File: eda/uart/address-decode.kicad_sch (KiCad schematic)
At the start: 2 parts, among them U6 74HCT139

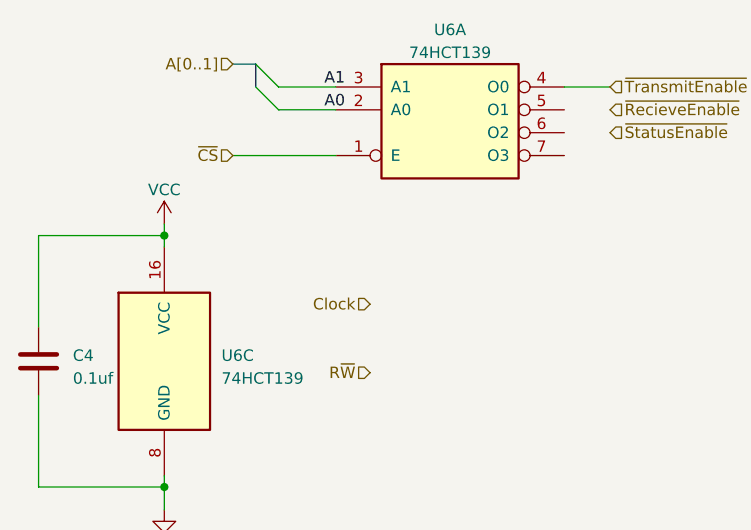
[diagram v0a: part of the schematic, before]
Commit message: Port main board schematic to kicad
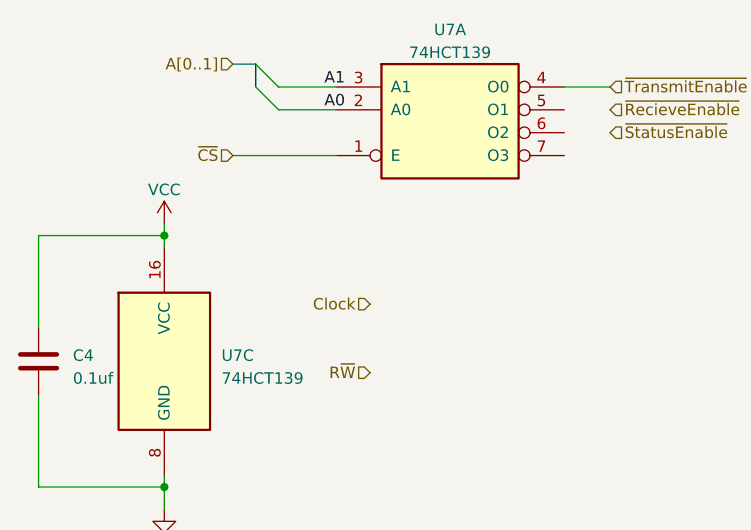
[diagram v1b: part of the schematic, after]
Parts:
- C4: footprint Capacitor_THT:C_Rect_L7.2mm_W2.5mm_P5.00mm_FKS2_FKP2_MKS2_MKP2 -> Capacitor_THT:C_Rect_L7.2mm_W3.5mm_P5.00mm_FKS2_FKP2_MKS2_MKP2
- renumbered U6 to U7
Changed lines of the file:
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@@
         )
         (path "/11545594-d6d6-4b37-a578-fa23933d5773/6450b7fb-1287-48ad-899d-2faf7b3277a5"
-          (reference "#PWR021") (unit 1)
+          (reference "#PWR023") (unit 1)
         )
       )
@@
         )
         (path "/11545594-d6d6-4b37-a578-fa23933d5773/6450b7fb-1287-48ad-899d-2faf7b3277a5"
-          (reference "#PWR022") (unit 1)
+          (reference "#PWR024") (unit 1)
         )
       )
@@
       (effects (font (size 1.27 1.27)) (justify left))
     )
-    (property "Footprint" "Capacitor_THT:C_Rect_L7.2mm_W2.5mm_P5.00mm_FKS2_FKP2_MKS2_MKP2" (at 20.0152 74.93 0)
+    (property "Footprint" "Capacitor_THT:C_Rect_L7.2mm_W3.5mm_P5.00mm_FKS2_FKP2_MKS2_MKP2" (at 20.0152 74.93 0)
       (effects (font (size 1.27 1.27)) hide)
     )
@@
         )
         (path "/11545594-d6d6-4b37-a578-fa23933d5773/6450b7fb-1287-48ad-899d-2faf7b3277a5"
-          (reference "C9") (unit 1)
+          (reference "C10") (unit 1)
         )
       )
@@
   (symbol (lib_id "74xx:74LS139") (at 33.02 71.12 0) (unit 3)
     (in_bom yes) (on_board yes) (dnp no) (fields_autoplaced)
-    (property "Reference" "U6" (at 39.37 70.485 0)
+    (property "Reference" "U7" (at 39.37 70.485 0)
       (effects (font (size 1.27 1.27)) (justify left))
     )
@@
       (project "uart"
         (path "/11545594-d6d6-4b37-a578-fa23933d5773/6450b7fb-1287-48ad-899d-2faf7b3277a5"
-          (reference "U6") (unit 3)
+          (reference "U7") (unit 3)
         )
       )
@@
   (symbol (lib_id "74xx:74LS139") (at 64.77 43.18 0) (unit 1)
     (in_bom yes) (on_board yes) (dnp no) (fields_autoplaced)
-    (property "Reference" "U6" (at 64.77 34.29 0)
+    (property "Reference" "U7" (at 64.77 34.29 0)
       (effects (font (size 1.27 1.27)))
     )
@@
       (project "uart"
         (path "/11545594-d6d6-4b37-a578-fa23933d5773/6450b7fb-1287-48ad-899d-2faf7b3277a5"
-          (reference "U6") (unit 1)
+          (reference "U7") (unit 1)
         )
       )

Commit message: Update eda
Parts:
- added U15: 74HCT00, symbol 74xx:74HCT00
- added U18: 74HCT32, Package_DIP:DIP-14_W7.62mm, symbol 74xx:74LS32
- added U2 (x3): 74HCT14, Package_DIP:DIP-14_W7.62mm, symbol 74xx:74LS14
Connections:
- net Clock: now also U15.2
- net R~{W}: now also U2.1
- net ~{CS}: now also U2.1; no longer U7.1 (E)
- net ~{RecieveEnable}: now also U18.3
- net ~{StatusEnable}: now also U18.6
- net at U7.5 (O1): now also U18.1
- net at U7.6 (O2): now also U18.4
- net ~{TransmitEnable}: no longer names the net of U7.4 (O0)
- net ~{TransmitEnable}: now also U2.1
- new net: U18.2, U18.5, U2.2
- new net: U15.1, U2.2
- new net: U15.3, U7.1 (E)
- new net TransmitEnable: U2.2
- no-connect marks 0 -> 1
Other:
- moved on the sheet: U7A

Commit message: Convert expansion breakout to kicad
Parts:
- U15: footprint (none) -> Package_DIP:DIP-14_W7.62mm
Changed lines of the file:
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@@
       (effects (font (size 1.27 1.27)))
     )
-    (property "Footprint" "" (at 83.82 42.545 0)
+    (property "Footprint" "Package_DIP:DIP-14_W7.62mm" (at 83.82 42.545 0)
       (effects (font (size 1.27 1.27)) hide)
     )

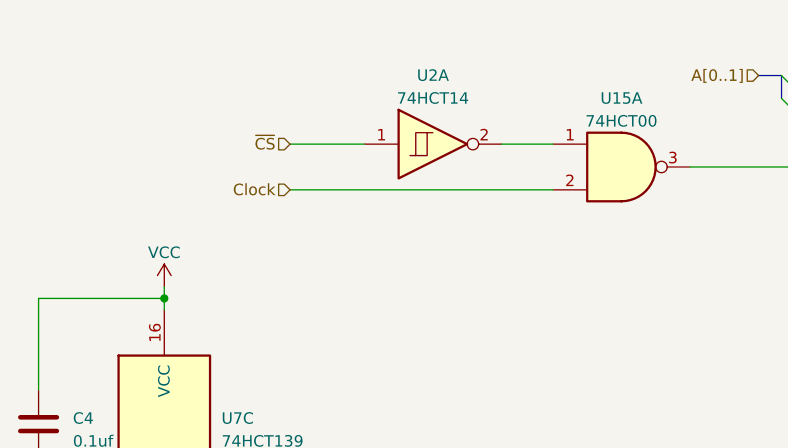
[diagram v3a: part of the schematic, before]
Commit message: Prelimary UART routing
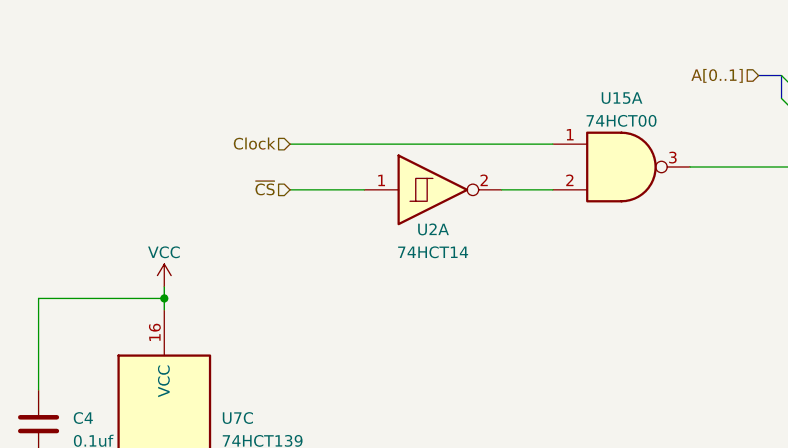
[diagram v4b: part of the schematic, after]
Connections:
- net Clock: now also U15.1; no longer U15.2
- net at U2.2: now also U15.2; no longer U15.1
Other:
- moved on the sheet: U2A
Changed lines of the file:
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@@
     (stroke (width 0) (type default))
   )
-  (wire (pts (xy 70.485 40.005) (xy 76.2 40.005))
+  (wire (pts (xy 70.485 45.085) (xy 76.2 45.085))
     (stroke (width 0) (type default))
   )
-  (wire (pts (xy 46.99 40.005) (xy 55.245 40.005))
+  (wire (pts (xy 46.99 45.085) (xy 55.245 45.085))
     (stroke (width 0) (type default))
   )
@@
     (stroke (width 0) (type default))
   )
-  (wire (pts (xy 46.99 45.085) (xy 76.2 45.085))
+  (wire (pts (xy 46.99 40.005) (xy 76.2 40.005))
     (stroke (width 0) (type default))
   )
@@
     (effects (font (size 1.27 1.27)) (justify left bottom))
   )
-  (hierarchical_label "~{CS}" (shape input) (at 46.99 40.005 180) (fields_autoplaced)
+  (hierarchical_label "~{CS}" (shape input) (at 46.99 45.085 180) (fields_autoplaced)
     (effects (font (size 1.27 1.27)) (justify right))
   )
-  (hierarchical_label "Clock" (shape input) (at 46.99 45.085 180) (fields_autoplaced)
+  (hierarchical_label "Clock" (shape input) (at 46.99 40.005 180) (fields_autoplaced)
     (effects (font (size 1.27 1.27)) (justify right))
   )
@@
     )
   )
-  (symbol (lib_id "74xx:74LS14") (at 62.865 40.005 0) (unit 1)
-    (in_bom yes) (on_board yes) (dnp no) (fields_autoplaced)
-    (property "Reference" "U2" (at 62.865 32.385 0)
+  (symbol (lib_id "74xx:74LS14") (at 62.865 45.085 0) (unit 1)
+    (in_bom yes) (on_board yes) (dnp no)
+    (property "Reference" "U2" (at 62.865 49.53 0)
       (effects (font (size 1.27 1.27)))
     )
-    (property "Value" "74HCT14" (at 62.865 34.925 0)
+    (property "Value" "74HCT14" (at 62.865 52.07 0)
       (effects (font (size 1.27 1.27)))
     )
-    (property "Footprint" "Package_DIP:DIP-14_W7.62mm" (at 62.865 40.005 0)
+    (property "Footprint" "Package_DIP:DIP-14_W7.62mm" (at 62.865 45.085 0)
       (effects (font (size 1.27 1.27)) hide)
     )
-    (property "Datasheet" "http://www.ti.com/lit/gpn/sn74LS14" (at 62.865 40.005 0)
+    (property "Datasheet" "http://www.ti.com/lit/gpn/sn74LS14" (at 62.865 45.085 0)
       (effects (font (size 1.27 1.27)) hide)
     )

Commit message: Normalize cap size
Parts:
- C4: footprint Capacitor_THT:C_Rect_L7.2mm_W3.5mm_P5.00mm_FKS2_FKP2_MKS2_MKP2 -> Capacitor_THT:C_Disc_D3.8mm_W2.6mm_P2.50mm
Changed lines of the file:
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@@
       (effects (font (size 1.27 1.27)) (justify left))
     )
-    (property "Footprint" "Capacitor_THT:C_Rect_L7.2mm_W3.5mm_P5.00mm_FKS2_FKP2_MKS2_MKP2" (at 20.0152 74.93 0)
+    (property "Footprint" "Capacitor_THT:C_Disc_D3.8mm_W2.6mm_P2.50mm" (at 20.0152 74.93 0)
       (effects (font (size 1.27 1.27)) hide)
     )

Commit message: Uart and loader work
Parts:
- renumbered C4 to C10
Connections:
- net R~{W}: now also U2.9; no longer U2.1
- net TransmitEnable: now also U2.10; no longer U2.2
- net at U18.2, U18.5: now also U2.8; no longer U2.2
- net at U7.4 (O0): now also U2.11; no longer U2.1

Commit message: Uart eda work
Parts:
- added U19: 74HCT74, Package_DIP:DIP-14_W7.62mm, symbol 74xx:74HC74
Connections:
- net VCC: now also U19.4 (~{S})
- net ~{DeviceEnable}: now reaches U15.3, U7.1 (E)
- net at U7.7 (O3): now also U19.3 (C)
- new net D0: U19.2 (D)
- new net IrqActive: U19.5 (Q)
- new net ~{RST}: U19.1 (~{R})
- no-connect marks 1 -> 0
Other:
- moved on the sheet: U15A, U2A, U2E, U7A

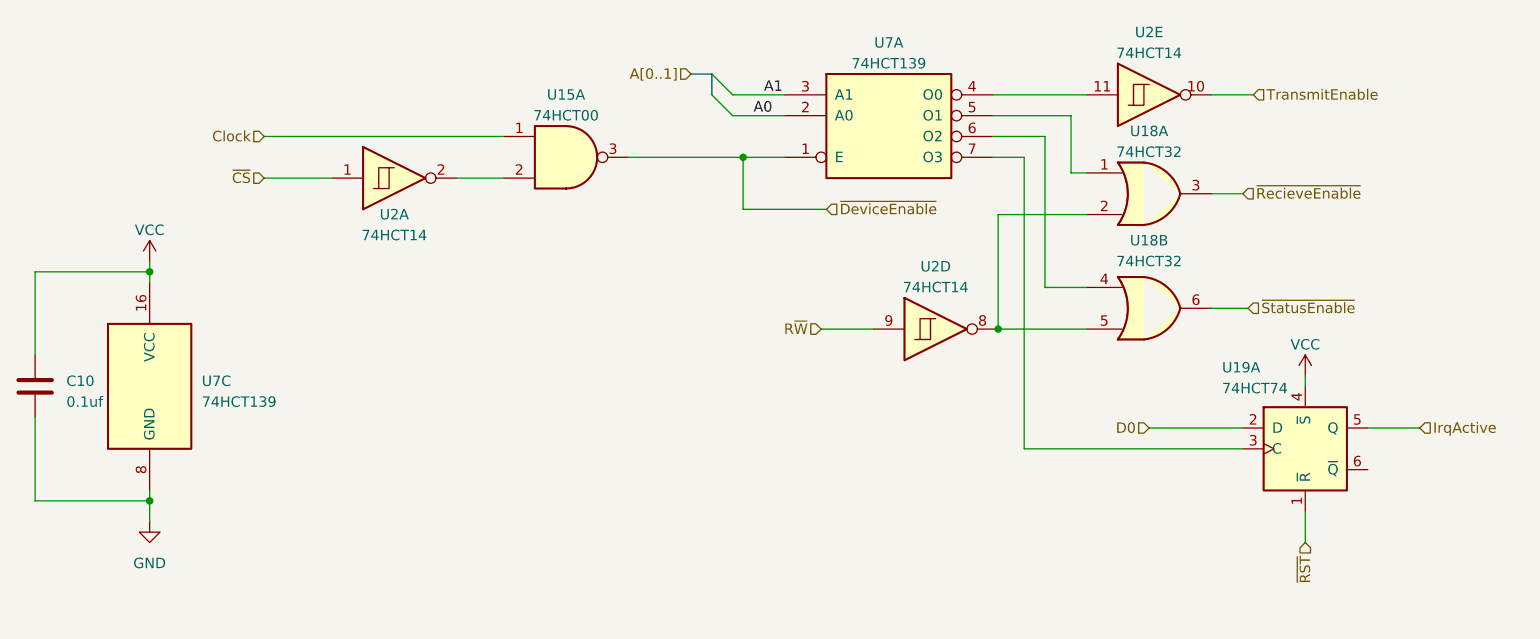
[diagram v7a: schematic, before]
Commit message: Add SPI
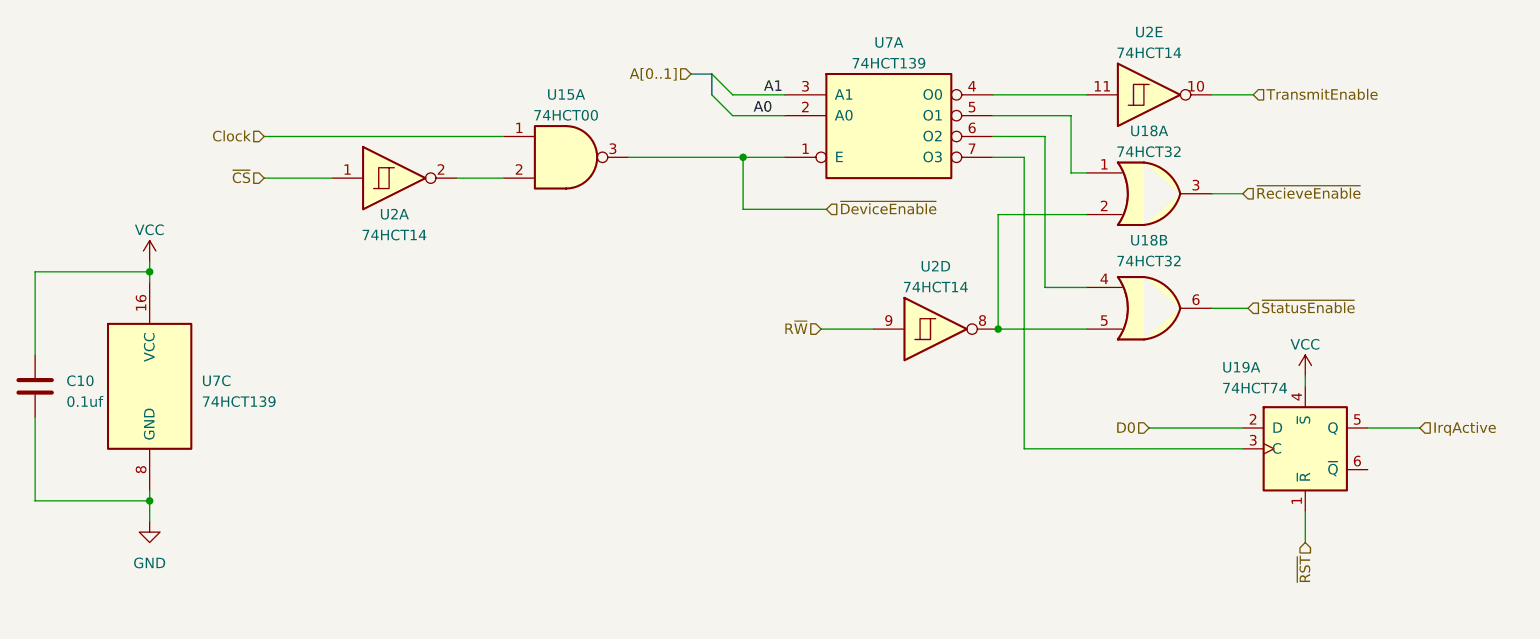
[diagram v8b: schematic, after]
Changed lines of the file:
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@@
 (kicad_sch
-	(version 20231120)
+	(version 20250114)
 	(generator "eeschema")
-	(generator_version "8.0")
+	(generator_version "9.0")
 	(paper "A4")
 	(junction
@@
 	(label "A0"
 		(at 106.68 38.1 0)
-		(fields_autoplaced yes)
 		(effects
 			(font
@@
 	(label "A1"
 		(at 107.95 35.56 0)
-		(fields_autoplaced yes)
 		(effects
 			(font
@@
 		(shape input)
 		(at 173.99 90.17 270)
-		(fields_autoplaced yes)
 		(effects
 			(font
@@
 		(shape input)
 		(at 115.57 49.53 0)
-		(fields_autoplaced yes)
 		(effects
 			(font
@@
 		(shape input)
 		(at 46.99 45.72 180)
-		(fields_autoplaced yes)
 		(effects
 			(font
@@
 		(shape input)
 		(at 187.96 76.2 0)
-		(fields_autoplaced yes)
 		(effects
 			(font
@@
 		(shape input)
 		(at 46.99 40.64 180)
-		(fields_autoplaced yes)
 		(effects
 			(font
@@
 		(shape input)
 		(at 154.94 76.2 180)
-		(fields_autoplaced yes)
 		(effects
 			(font
@@
 		(shape input)
 		(at 167.64 35.56 0)
-		(fields_autoplaced yes)
 		(effects
 			(font
@@
 		(shape input)
 		(at 114.935 64.135 180)
-		(fields_autoplaced yes)
 		(effects
 			(font
@@
 		(shape input)
 		(at 99.06 33.02 180)
-		(fields_autoplaced yes)
 		(effects
 			(font
@@
 		(shape input)
 		(at 167.005 61.595 0)
-		(fields_autoplaced yes)
 		(effects
 			(font
@@
 		(shape input)
 		(at 166.37 47.625 0)
-		(fields_autoplaced yes)
-		(effects
-			(font
+		(effects
+			(font
